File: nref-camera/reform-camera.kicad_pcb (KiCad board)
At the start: 4 copper layers, 44 x 44 mm, 185 parts, among them J1 USB_C_Receptacle, J2 Conn_01x04, J3 Conn_ARM_JTAG_SWD_10, J4 Conn_01x24, U1 PCMF1USB3BC, U10 TLV71733P, U11 FAN53611AUC12X, U12 FAN53600AUC28X, U13 CYUSB306X, U14 FAN53611AUC18X, U15 TLV71715P, U16 TPS2290x, U17 TPS2290x, U18 SN74LVC1T45YZP, U19 SN74LVC1T45YZP, U2 PCMF1USB3BC, U20 SN74LVC1T45YZP, U21 74LVC2G17, U3 AT25FF041A-UUN-T, U4 TLV40x1, U5 PCMF1USB3BC, U6 PCMF1USB3BC, U7 SN74LVC1T45YZP, U8 SN74LVC1T45YZP, U9 TMUXHS4212, X1 ECS-1618-240-BN-TR, X2 NZ2520SB-32.768KHZ-NSA3534C, X3 ECS-1618-192-BN-TR

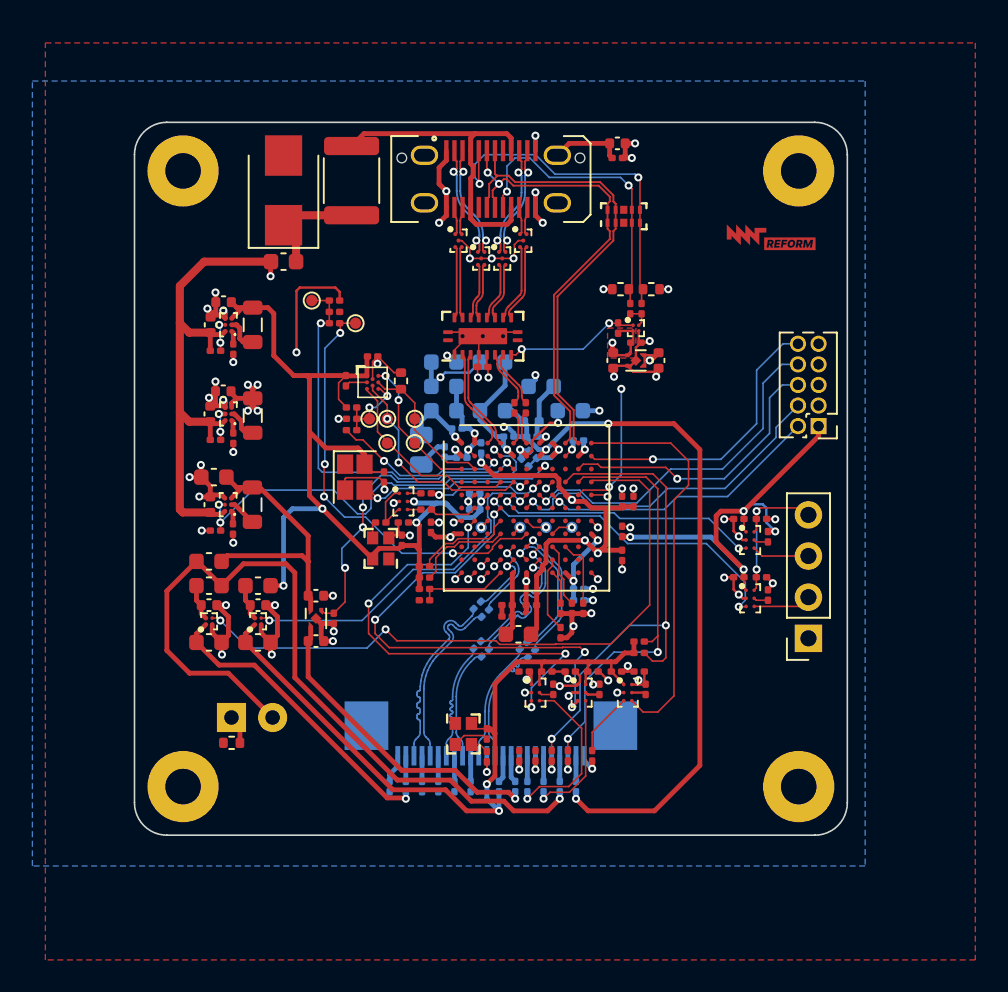
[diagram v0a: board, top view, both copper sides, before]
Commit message: camera: redesigned and fully routed
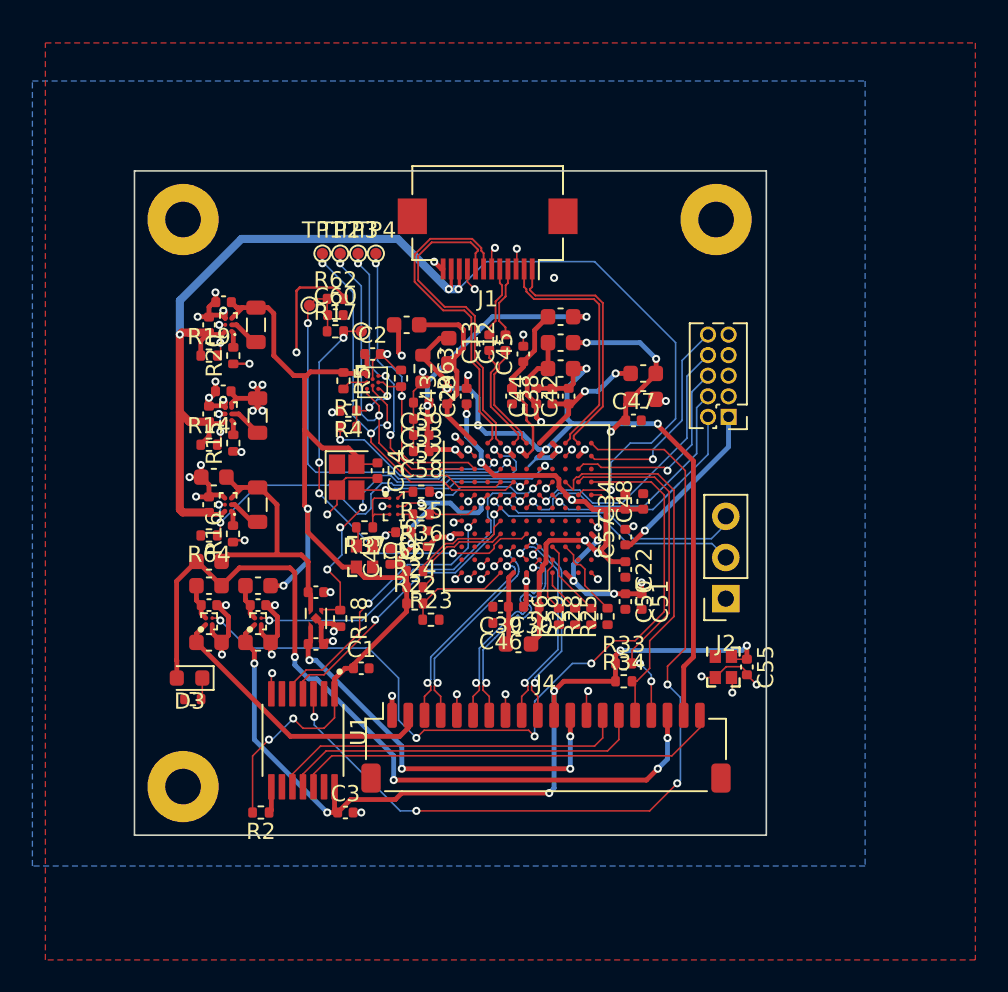
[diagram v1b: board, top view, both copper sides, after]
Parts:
- removed C10, C26, C27, C28, C31, C32, C33, C4, C5, C7, C8: 0.1u, Capacitor_SMD:C_0201_0603Metric
- removed C6, C9: 1u, Capacitor_SMD:C_0402_1005Metric
- removed D1: ESD7104, reform-camera:ON_Semi_UDFN10_517BB
- removed D2: SMAJ5.0A, Diode_SMD:D_SMB
- removed F1: Polyfuse_Small, Fuse:Fuse_1812_4532Metric
- removed FB1: FerriteBead_Small, Capacitor_SMD:C_0603_1608Metric
- removed G***: LOGO, reform-camera:mntreform-5mm-copper
- removed G***: LOGO, reform-camera:reform2-camera
- removed H4: MountingHole_Pad, MountingHole:MountingHole_2.2mm_M2_Pad
- removed R10, R9: 5k1, Resistor_SMD:R_0402_1005Metric
- removed R11, R12, R13, R30, R31, R32: 10k, Resistor_SMD:R_0201_0603Metric
- removed R3: 100k, Resistor_SMD:R_0201_0603Metric
- removed R38, R39, R40, R41, R42, R43, R44, R45, R46, R47, R48, R49, R50, R51, R52, R53, R54, R55, R56, R57, R58, R59, R6, R60, R61, R7: 0R, Resistor_SMD:R_0201_0603Metric
- removed TP11, TP6, TP7, TP8, TP9: TestPoint, reform-camera:TestPoint_Pad_D0.7mm
- removed U10: TLV71733P, Package_DFN_QFN:UDFN-4-1EP_1x1mm_P0.65mm_EP0.48x0.48mm
- removed U18, U19, U20, U7, U8: SN74LVC1T45YZP, reform-camera:Texas-DSBGA6_2x3_1.39x0.9mm_YZP
- removed U2, U5, U6: PCMF1USB3BC, reform-camera:Nexperia-WLCSP5_2-1-2_0.77x1.17mm
- removed U4: TLV40x1, reform-camera:Texas-DSBGA4_2x2_0.73x0.73mm_YKA
- removed U9: TMUXHS4212, reform-camera:Texas-VQFN20_2.5x4.5mm_RKS
- C1: value 1n -> 0.1uF
- C12, C13, C2, C22, C25, C30, C34, C39, C46, C48, C49, C54, C55, C56, C57, C60: footprint Capacitor_SMD:C_0201_0603Metric -> Capacitor_SMD:C_0402_1005Metric
- C21, C35, C36, C37: moved to F.Cu
- C29, C38, C42, C43, C44, C45, C47, C50, C51, C52, C53, C58, C59: footprint Capacitor_SMD:C_0201_0603Metric -> Capacitor_SMD:C_0402_1005Metric; moved to F.Cu
- C3: value 0.1u -> 0.1uF; footprint Capacitor_SMD:C_0201_0603Metric -> Capacitor_SMD:C_0402_1005Metric
- D3: footprint LED_THT:LED_D3.0mm -> LED_SMD:LED_0603_1608Metric; moved to F.Cu
- FB2, FB3, FB4: value FerriteBead_Small -> 300Ohm@100MHz, 2A
- FB5, FB6, FB7, FB8: value 600Ohm@100MHz, 2A -> 300Ohm@100MHz, 2A; moved to F.Cu
- FB9: value 600Ohm@100MHz, 2A -> 300Ohm@100MHz, 2A
- J1: value USB_C_Receptacle -> Conn_01x12_Pin; footprint Connector_USB:USB_C_Receptacle_JAE_DX07S024WJ3R400 -> Connector_FFC-FPC:Hirose_FH12-12S-0.5SH_1x12-1MP_P0.50mm_Horizontal
- J2: value Conn_01x04 -> Conn_01x03; footprint Connector_PinSocket_2.54mm:PinSocket_1x04_P2.54mm_Vertical -> Connector_PinSocket_2.54mm:PinSocket_1x03_P2.54mm_Vertical
- J4: value Conn_01x24 -> Conn_01x20; footprint reform-camera:FPC_24 -> Connector_JST:JST_SH_SM20B-SRSS-TB_1x20-1MP_P1.00mm_Horizontal; moved to F.Cu
- R1, R14, R15, R16, R17, R18, R19, R20, R22, R23, R24, R25, R26, R27, R28, R29, R33, R34, R35, R36, R37, R4, R5, R62, R64: footprint Resistor_SMD:R_0201_0603Metric -> Resistor_SMD:R_0402_1005Metric
- R2: value 200k -> 1k; footprint Resistor_SMD:R_0201_0603Metric -> Resistor_SMD:R_0402_1005Metric
- R63: footprint Resistor_SMD:R_0805_2012Metric -> Resistor_SMD:R_0603_1608Metric; moved to F.Cu
- U1: value PCMF1USB3BC -> TXS0104EPWRG4; footprint reform-camera:Nexperia-WLCSP5_2-1-2_0.77x1.17mm -> reform-camera:SOP65P640X120-14N
- moved R2 46.0 mm to (191.8, 102.6), turned to 180 degrees
- moved C1 36.1 mm to (198.0, 93.7)
- moved C3 34.1 mm to (197.0, 102.6)
- moved U1 31.7 mm to (194.4, 98.1), turned to -90 degrees
- moved C55 16.6 mm to (221.8, 93.6)
- moved X1 16.6 mm to (220.3, 93.6)
- moved C21 12.5 mm to (215.4, 77.1)
- moved TP3 12.2 mm to (197.8, 68.1), turned to 0 degrees
- moved TP2 12.1 mm to (196.7, 68.1), turned to 0 degrees
- moved TP1 11.0 mm to (195.6, 68.1), turned to 0 degrees
- moved TP4 10.2 mm to (198.9, 68.1), turned to 0 degrees
- moved FB5 6.35 mm to (215.4, 75.5), turned to 180 degrees
- moved C45 6.23 mm to (208.0, 74.3), turned to 90 degrees
- moved H1 5.92 mm to (219.9, 66.0)
- moved FB8 5.83 mm to (210.3, 72.0)
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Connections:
- C1 pad 1: Net-(C1-Pad1) -> +1V8
- C12 pad 2: /SSTX- -> USB_TXN
- C13 pad 2: /SSTX+ -> USB_TXP
- C3 pad 1: +3V3 -> /CAM_DOVDD
- J2 pad 2: /UART_RX -> /UART_RX_CX3
- J2 pad 3: /UART_TX -> /UART_TX_CX3
- J3 pad 7: (no net) -> unconnected-(J3-KEY-Pad7)
- J4 pad 1: Net-(J4-Pad1) -> GND
- J4 pad 10: Net-(J4-Pad10) -> /CAM_MIPI_D1P
- J4 pad 11: /D1N -> /CAM_DOVDD
- J4 pad 12: Net-(J4-Pad12) -> /CAM_DVDD
- J4 pad 13: /D1P -> /CAM_MCLK
- J4 pad 14: Net-(J4-Pad14) -> /CAM_PWDNB
- J4 pad 15: Net-(J4-Pad15) -> /CAM_RST
- J4 pad 16: Net-(J4-Pad16) -> /CAM_SCL
- J4 pad 17: Net-(J4-Pad17) -> /CAM_SDA
- J4 pad 18: Net-(J4-Pad18) -> /CAM_AVDD
- J4 pad 19: Net-(J4-Pad19) -> GNDA
- J4 pad 2: Net-(J4-Pad2) -> /CAM_AF_VCC
- J4 pad 20: Net-(J4-Pad20) -> /CAM_STROBE
- J4 pad 3: /D0N -> /CAM_MIPI_D0N
- J4 pad 4: Net-(J4-Pad4) -> /CAM_MIPI_D0P
- J4 pad 5: /D0P -> GND
- J4 pad 6: Net-(J4-Pad6) -> /CAM_MIPI_CN
- J4 pad 7: /CN -> /CAM_MIPI_CP
- J4 pad 8: Net-(J4-Pad8) -> GND
- J4 pad 9: /CP -> /CAM_MIPI_D1N
- R1 pad 2: Net-(R1-Pad2) -> Net-(U3-~{WP})
- R2 pad 1: Net-(C1-Pad1) -> Net-(U1-OE)
- R2 pad 2: GND -> +1V8
- R4 pad 1: Net-(R1-Pad2) -> Net-(U3-~{WP})
- TP4 pad 1: Net-(R1-Pad2) -> /MISO
- U13 pad A10: /USB_D- -> USB_D-
- U13 pad A3: /SSRX- -> USB_RXN
- U13 pad A4: /SSRX+ -> USB_RXP
- U13 pad A9: /USB_D+ -> USB_D+
- U13 pad C11: (no net) -> unconnected-(U13A-I2S_MCLK/GPIO57-PadC11)
- U13 pad C4: (no net) -> unconnected-(U13A-GPIO26-PadC4)
- U13 pad C6: (no net) -> unconnected-(U13A-GPIO18-PadC6)
- U13 pad C8: (no net) -> unconnected-(U13A-GPIO22-PadC8)
- U13 pad C9: (no net) -> unconnected-(U13A-GPIO45-PadC9)
- U13 pad D1: (no net) -> unconnected-(U13A-I2S_CLK/GPIO50-PadD1)
- U13 pad D2: (no net) -> unconnected-(U13A-I2S_SD/GPIO51-PadD2)
- U13 pad D3: (no net) -> unconnected-(U13A-I2S_WS/GPIO52-PadD3)
- U13 pad E1: (no net) -> unconnected-(U13A-UART_CTS/GPIO47-PadE1)
- U13 pad F1: (no net) -> unconnected-(U13A-DNU-PadF1)
- U13 pad F10: (no net) -> unconnected-(U13A-DNU-PadF10)
- U13 pad F3: (no net) -> unconnected-(U13A-GPIO44-PadF3)
- U13 pad F5: (no net) -> unconnected-(U13A-UART_RTS/GPIO46-PadF5)
- U13 pad F7: (no net) -> unconnected-(U13A-DNU-PadF7)
- U13 pad F8: (no net) -> unconnected-(U13A-DNU-PadF8)
- U13 pad F9: (no net) -> unconnected-(U13A-DNU-PadF9)
- U13 pad G10: (no net) -> unconnected-(U13A-DNU-PadG10)
- U13 pad G3: Net-(TP6-Pad1) -> unconnected-(U13D-MCLK-PadG3)
- U13 pad G5: (no net) -> unconnected-(U13A-GPIO25-PadG5)
- U13 pad G6: Net-(TP8-Pad1) -> unconnected-(U13D-HSYNC_test-PadG6)
- U13 pad G7: (no net) -> unconnected-(U13A-DNU-PadG7)
- U13 pad G8: (no net) -> unconnected-(U13A-DNU-PadG8)
- U13 pad G9: (no net) -> unconnected-(U13A-DNU-PadG9)
- U13 pad H10: (no net) -> unconnected-(U13A-DNU-PadH10)
- U13 pad H2: (no net) -> unconnected-(U13A-DNU-PadH2)
- U13 pad H3: (no net) -> unconnected-(U13A-DNU-PadH3)
- U13 pad H5: Net-(TP7-Pad1) -> unconnected-(U13D-VSYNC_test-PadH5)
- U13 pad H7: (no net) -> unconnected-(U13A-DNU-PadH7)
- U13 pad H8: Net-(TP9-Pad1) -> unconnected-(U13D-PCLK_test-PadH8)
- U13 pad H9: (no net) -> unconnected-(U13A-DNU-PadH9)
- U13 pad J1: (no net) -> unconnected-(U13A-DNU-PadJ1)
- U13 pad J10: (no net) -> unconnected-(U13A-DNU-PadJ10)
- U13 pad J2: (no net) -> unconnected-(U13A-DNU-PadJ2)
- U13 pad J3: (no net) -> unconnected-(U13A-DNU-PadJ3)
- U13 pad J4: (no net) -> unconnected-(U13A-DNU-PadJ4)
- U13 pad K1: (no net) -> unconnected-(U13A-DNU-PadK1)
- U13 pad K10: (no net) -> unconnected-(U13A-DNU-PadK10)
- U13 pad K11: (no net) -> unconnected-(U13A-DNU-PadK11)
- U13 pad K2: (no net) -> unconnected-(U13A-DNU-PadK2)
- U13 pad K9: (no net) -> unconnected-(U13A-DNU-PadK9)
- U13 pad L10: (no net) -> unconnected-(U13A-DNU-PadL10)
- U3 pad E3: Net-(R1-Pad2) -> Net-(U3-~{WP})
- X1 pad 1: (no net) -> unconnected-(X1-Tri-State-Pad1)
- X2 pad 1: (no net) -> unconnected-(X2-Tri-State-Pad1)
- X3 pad 1: (no net) -> unconnected-(X3-Tri-State-Pad1)
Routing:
- net GND: track 113.6 -> 77.3 mm, vias 78 -> 55
- net /CAM_STROBE_CX3: track 24.6 -> 53.9 mm, vias 0 -> 4
- net /USB_D-: track 28.9 -> 0.00 mm
- net /USB_D+: track 28.7 -> 0.00 mm, vias 2 -> 0
- net /CAM_STROBE: track 3.89 -> 26.6 mm
- net /CC1: track 22.3 -> 0.00 mm, vias 2 -> 0
- net USB_RXN: track 0.00 -> 20.6 mm
- net Net-(F1-Pad1): track 20.1 -> 0.00 mm
- net USB_RXP: track 0.00 -> 19.9 mm
- net Net-(C1-Pad1): track 19.0 -> 0.00 mm
- net /CC2: track 18.5 -> 0.00 mm, vias 2 -> 0
- net USB_D+: track 0.00 -> 15.7 mm
- net USB_D-: track 0.00 -> 15.7 mm
- net /CAM_RST: track 8.26 -> 22.7 mm, vias 1 -> 0
- net +3V3: track 14.2 -> 0.00 mm, vias 2 -> 0
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- removed copper zone on F.Cu, net +3V3
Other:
- board size 44 x 44 mm -> 39 x 41 mm

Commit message: camera: d-3 done, off to board house
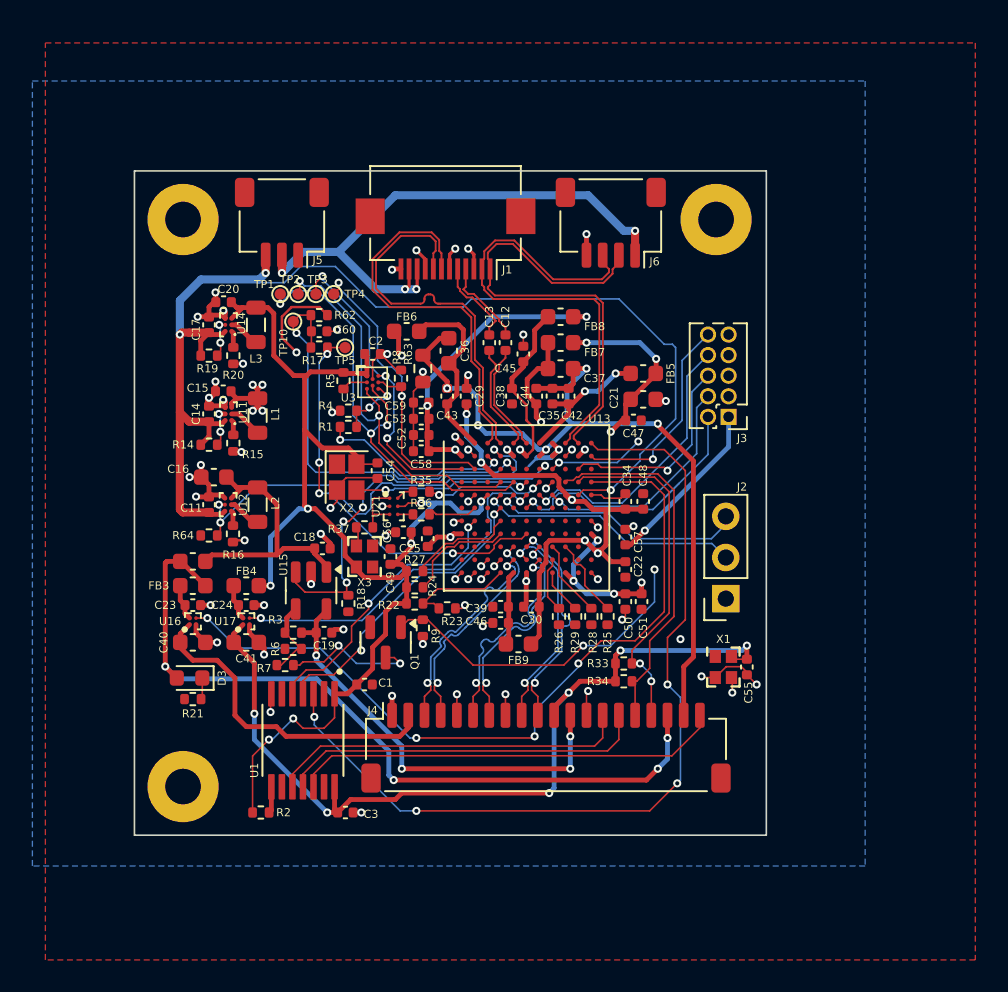
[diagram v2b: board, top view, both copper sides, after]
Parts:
- added H4: BADGE, reform-camera:nref-camera-badge, B.Cu at (194.2, 83.6)
- added J5: Conn_01x03, Connector_JST:JST_SH_SM03B-SRSS-TB_1x03-1MP_P1.00mm_Horizontal, F.Cu at (193.1, 66.2)
- added J6: USB_INT1, Connector_JST:JST_SH_SM04B-SRSS-TB_1x04-1MP_P1.00mm_Horizontal, F.Cu at (213.4, 66.2)
- added Q1: AO3416, Package_TO_SOT_SMD:SOT-23, F.Cu at (199.5, 92.1)
- added R3: 20k, Resistor_SMD:R_0402_1005Metric, F.Cu at (193.8, 91.5)
- added R6: 16.9k, Resistor_SMD:R_0402_1005Metric, F.Cu at (193.8, 92.5)
- added R7: 36.5k, Resistor_SMD:R_0402_1005Metric, F.Cu at (193.3, 93.5)
- added R9: 10k, Resistor_SMD:R_0402_1005Metric, F.Cu at (201.8, 91.2)
- U15: value TLV71715P -> TLV75801PDBV; footprint Package_DFN_QFN:UDFN-4-1EP_1x1mm_P0.65mm_EP0.48x0.48mm -> Package_TO_SOT_SMD:SOT-23-5
- moved TP3 3.61 mm to (195.2, 70.6)
- moved TP1 3.61 mm to (193.0, 70.6)
- moved TP2 3.61 mm to (194.1, 70.6)
- moved TP4 3.61 mm to (196.3, 70.6)
- moved C18 2.73 mm to (195.6, 86.3)
- moved J1 2.60 mm to (203.2, 67.2)
- moved U15 1.75 mm to (194.9, 88.9), turned to -90 degrees
- moved C60 1.41 mm to (195.4, 72.9)
- moved R17 1.41 mm to (195.4, 73.9)
- moved R62 1.41 mm to (195.4, 71.9)
- moved TP10 1.41 mm to (193.8, 72.3)
- moved TP5 1.41 mm to (197.0, 73.9)
- moved R23 1.22 mm to (203.3, 90.0)
- moved R18 1.05 mm to (197.2, 89.7)
- moved C1 1.02 mm to (198.2, 94.7)
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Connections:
- J1 pad 10: VBUS -> +5V
- J1 pad 11: VBUS -> +5V
- U13 pad C8: unconnected-(U13A-GPIO22-PadC8) -> /DVDD_1V5_SEL
- U15 pad 1: /CAM_DVDD -> +2V8
- U15 pad 4: +2V8 -> Net-(U15-FB)
- U15 pad 5: GND -> /CAM_DVDD
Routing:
- net /DVDD_1V5_SEL: track 0.00 -> 35.6 mm, vias 0 -> 4
- net +5V: track 0.00 -> 35.4 mm, vias 0 -> 4
- net USB_D+: track 15.7 -> 29.8 mm
- net USB_D-: track 15.7 -> 29.8 mm
- net Net-(Q1-D): track 0.00 -> 8.65 mm, vias 0 -> 2
- net Net-(U15-FB): track 0.00 -> 5.10 mm
- net VBUS: track 77.6 -> 73.5 mm, vias 4 -> 3
- net USB_RXP: track 19.9 -> 23.9 mm
- net GND: track 77.3 -> 73.7 mm, vias 55 -> 61
- net USB_RXN: track 20.6 -> 24.0 mm
- net /CAM_AF_VCC: track 17.9 -> 20.3 mm
- net /CAM_AVDD: track 50.7 -> 48.6 mm
- net /CAM_DVDD: track 25.1 -> 26.9 mm
- net /DVDD_SUPPLY_EN: track 22.6 -> 24.4 mm
- net +1V2: track 65.2 -> 63.5 mm
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
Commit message: add latest PCB updates
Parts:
- added H5: MountingHole_Pad, MountingHole:MountingHole_2.2mm_M2_Pad, F.Cu at (227.0, 101.0)
- added R10: 0R, Resistor_SMD:R_0402_1005Metric, F.Cu at (191.6, 67.1)
- added R11: 10k, Resistor_SMD:R_0402_1005Metric, F.Cu at (197.3, 81.7)
- C11, C14, C17, C35: value 2.2u -> 2.2uF
- C12, C13, C2, C22, C29, C30, C42, C43, C44, C45, C46, C47, C48, C49, C51, C54, C55, C56, C57, C58, C59, C60: value 0.1u -> 0.1uF
- C15, C20: value 4.7u -> 4.7uF
- C16, C40, C41: value 10u -> 10uF
- C18, C19, C23, C24: value 1u -> 1uF
- C21, C36, C37: value 22u -> 22uF
- C25, C34, C38, C39, C50, C52, C53: value 0.01u -> 0.01uF
- moved H4 23.4 mm to (207.0, 64.0), turned to 0 degrees
- moved H1 8.68 mm to (227.0, 61.0)
- moved H2 5.00 mm to (187.0, 61.0)
- moved C1 2.83 mm to (201.0, 94.9)
- moved C15 2.83 mm to (192.3, 76.8)
- moved C19 2.83 mm to (198.5, 91.7)
- moved C2 2.83 mm to (201.5, 74.5)
- moved C52 2.83 mm to (204.5, 79.5)
- moved C53 2.83 mm to (204.5, 78.5)
- moved C58 2.83 mm to (204.5, 80.5)
- moved C59 2.83 mm to (204.5, 77.5)
- moved FB9 2.83 mm to (210.5, 92.4)
- moved R1 2.83 mm to (200.0, 79.0)
- moved R18 2.83 mm to (200.0, 89.9)
- moved R25 2.83 mm to (216.0, 90.7)
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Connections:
- J1 pad 4: USB_TXN -> USB_RXN
- J1 pad 5: USB_TXP -> USB_RXP
- J1 pad 7: USB_RXN -> USB_TXN
- J1 pad 8: USB_RXP -> USB_TXP
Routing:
- net +5V: track 35.4 -> 41.3 mm
- net VBUS: track 73.5 -> 78.9 mm
- net USB_RXN: track 24.0 -> 19.5 mm, vias 0 -> 2
- net USB_RXP: track 23.9 -> 19.5 mm, vias 0 -> 2
- net GND: track 73.7 -> 76.6 mm, vias 61 -> 90
- net USB_TXP: track 5.41 -> 7.29 mm
- net USB_TXN: track 5.41 -> 7.29 mm
- net +1V8: track 138.6 -> 140.3 mm
- net Net-(U13D-MIPI_RESET): track 25.3 -> 26.6 mm
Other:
- board size 39 x 41 mm -> 46 x 46 mm
